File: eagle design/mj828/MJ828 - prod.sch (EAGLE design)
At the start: 34 parts, among them IC1 ATTINY4313-MMH, IC2 PBRC8.00GR50X000, IC3 LDK320M50R, IC4 MCP2515, IC5 MCP2561-2, IC6 MAX6817EUT+T, IC7 MAX6817EUT+T, SW1 TL3305CF160QG, SW2 TL3305CF160QG

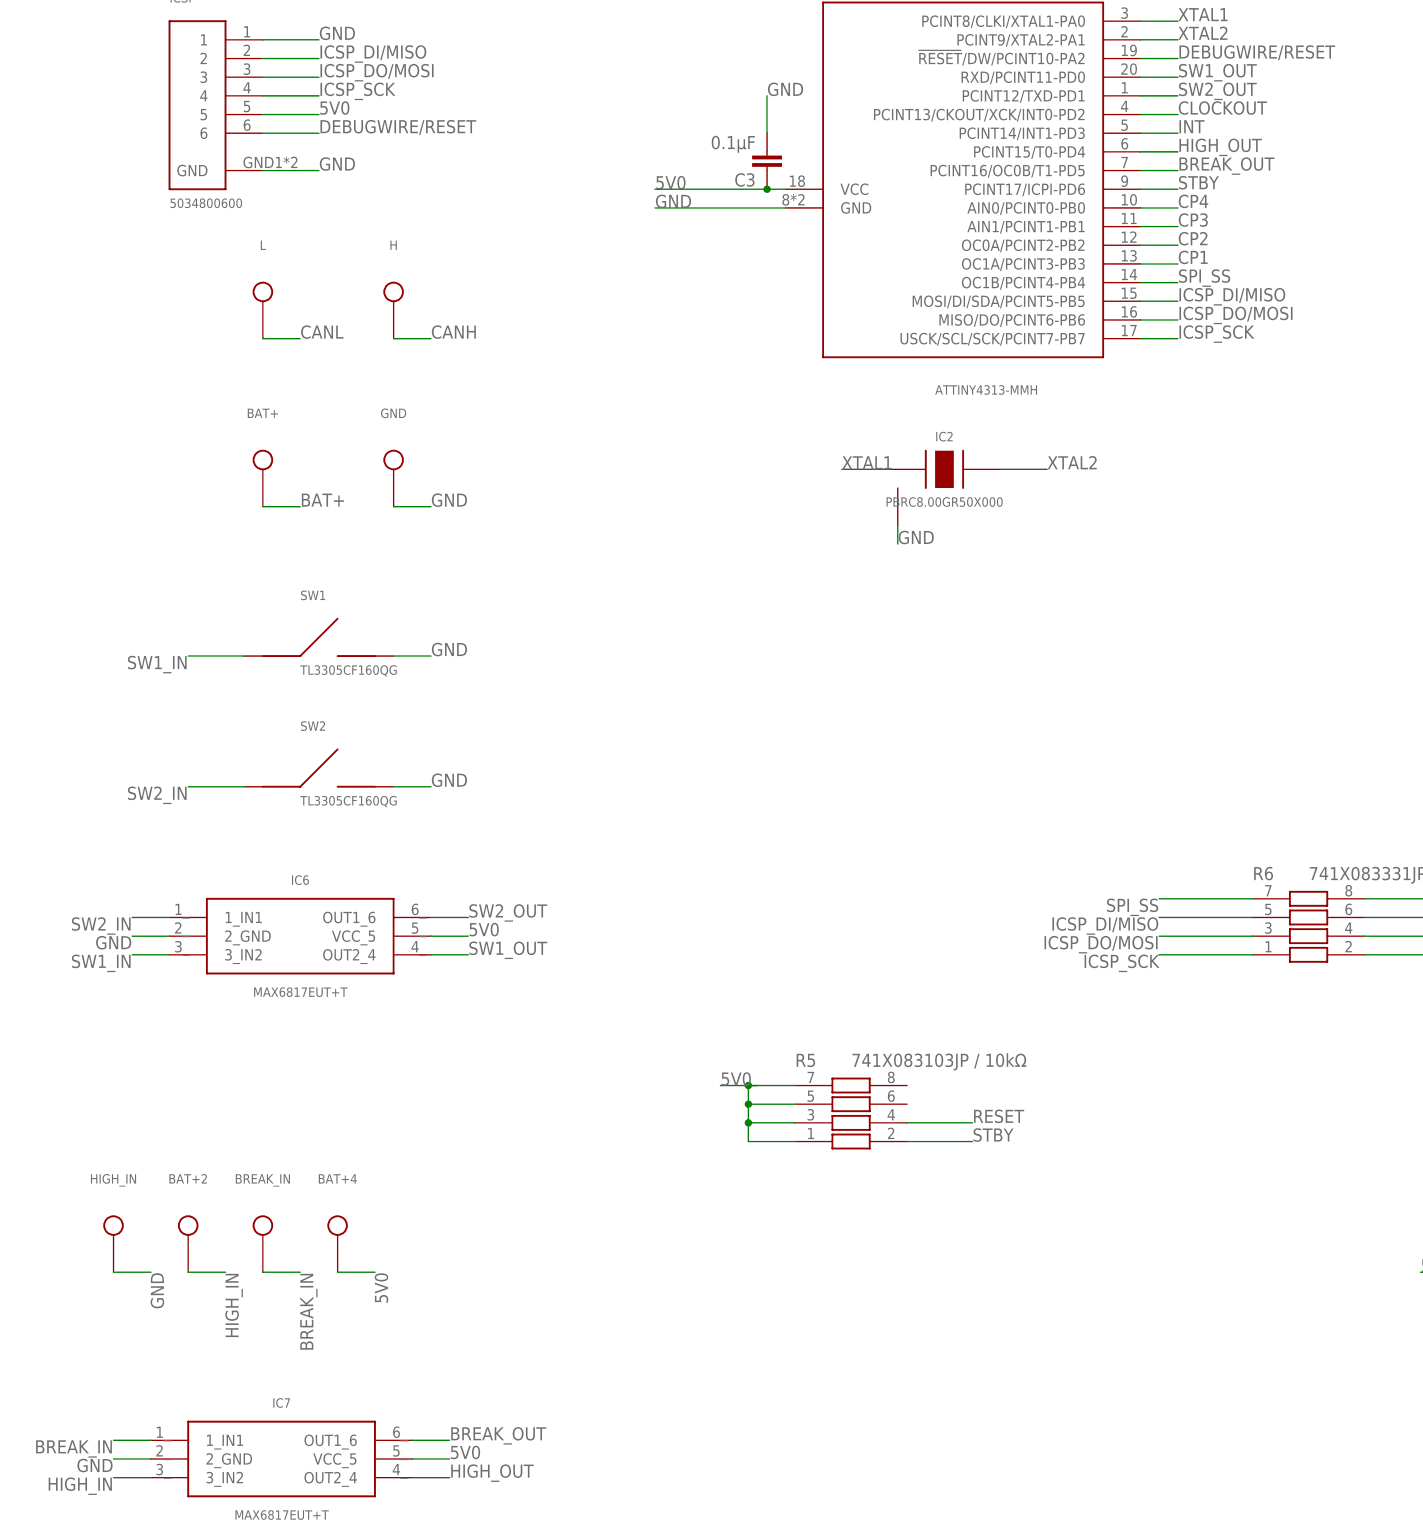
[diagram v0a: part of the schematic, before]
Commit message: MJ828 rev.2 board finished - added 104249/104250 mezzanine connector in order to avoid soldering wires directly onto PCB - drew mezzanine FPC - added datasheets & libraries for molex 104249/104250 mezzanine connectors
replaced hall effect sensor for brake lever FPC
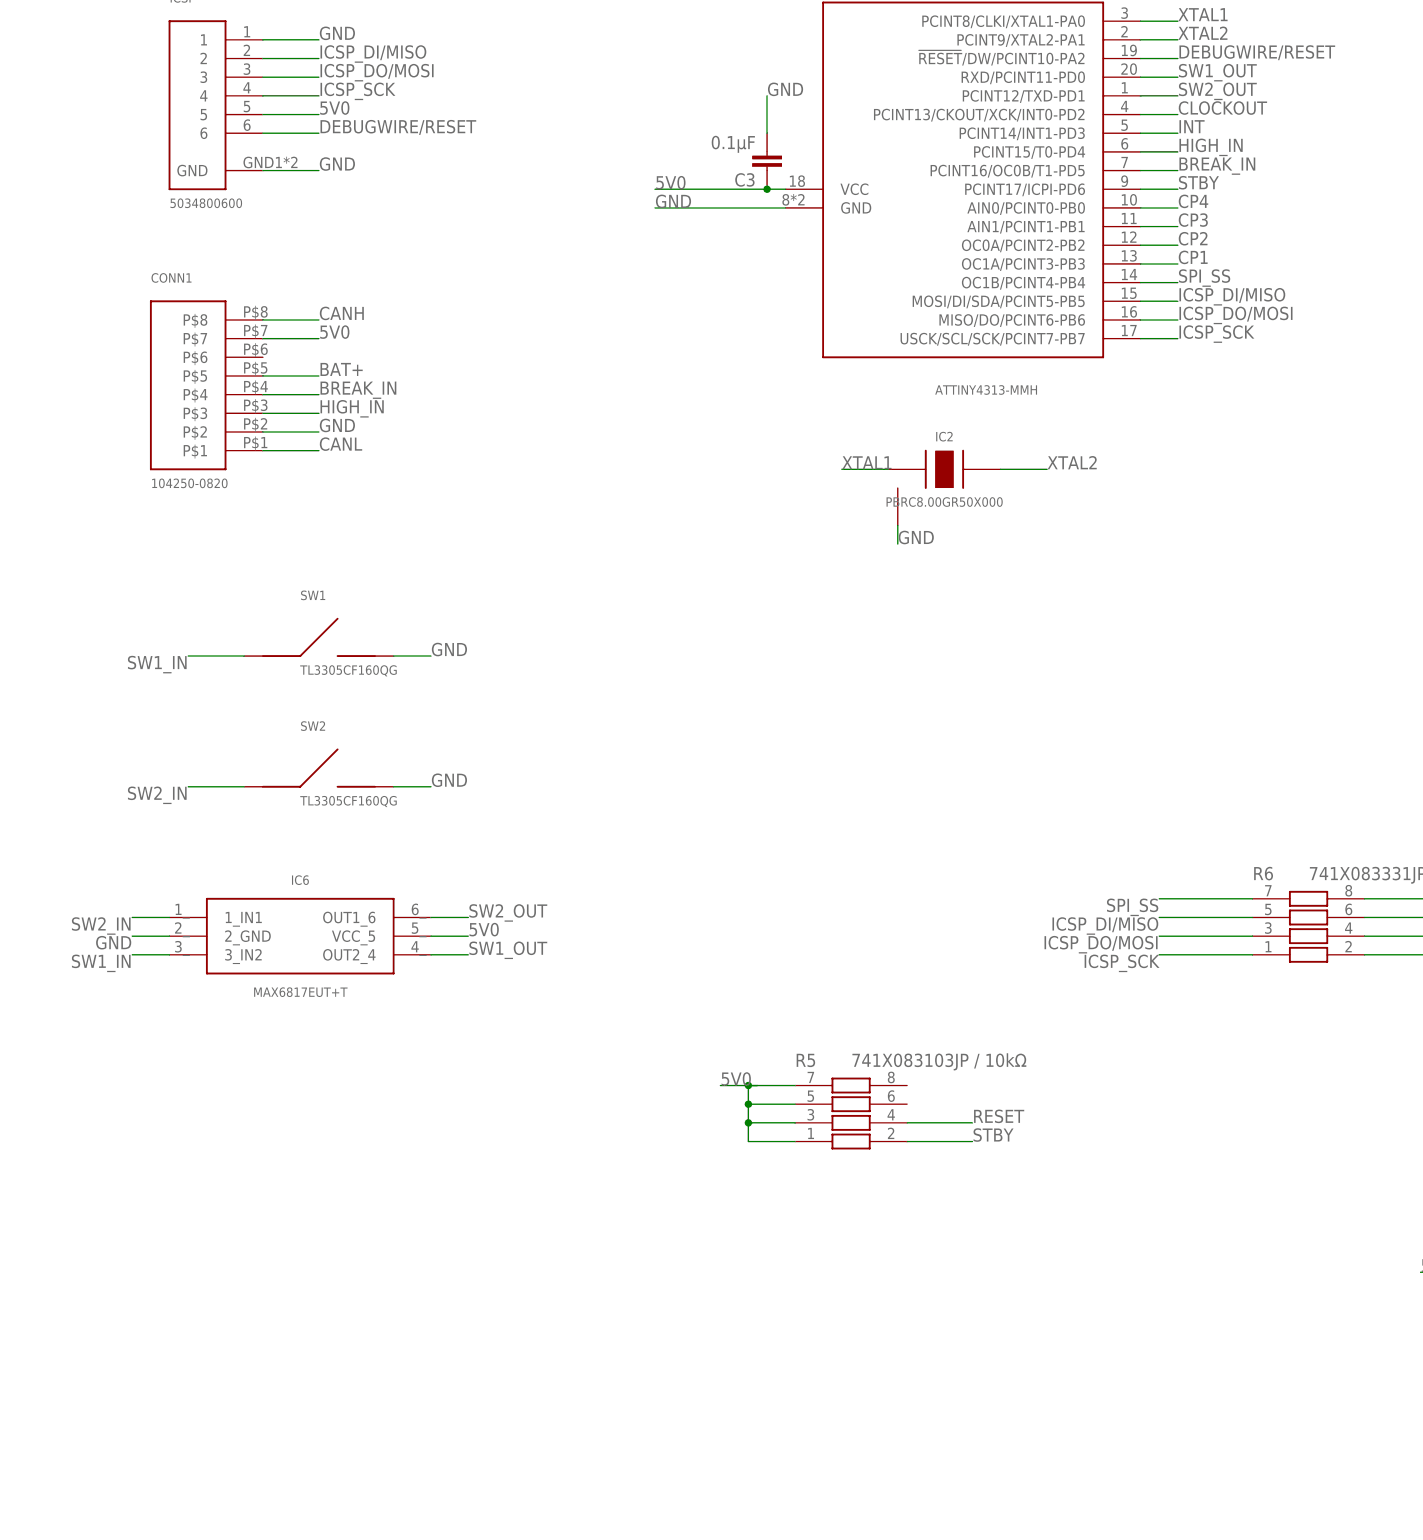
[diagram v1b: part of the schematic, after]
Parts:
- removed BAT+, BAT+2, BAT+4, BREAK_IN, HIGH_IN: 8V4 Battery +, signal testpoint:TPTH-0.9MM
- removed GND: Ground, signal testpoint:TPTH-0.9MM
- removed H: CAN High, signal testpoint:TPTH-0.9MM
- removed IC7: MAX6817EUT+T, MAX6817EUT - CMOS Switch debouncer:MAX6817EUT
- removed L: CAN Low, signal testpoint:TPTH-0.9MM
- added CONN1: 104250-0820, 1042500820 - Board to Board Connector, 8p - Header:104250-0820
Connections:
- removed net BREAK_OUT: IC1.PCINT16/OC0B/T1-PD5, IC7.OUT1_6
- removed net HIGH_OUT: IC1.PCINT15/T0-PD4, IC7.OUT2_4
- net 5V0: now also CONN1.P$7; no longer BAT+4.TP$1, IC7.VCC_5
- net BAT+: now also CONN1.P$5; no longer BAT+.TP$1
- net BREAK_IN: now also CONN1.P$4, IC1.PCINT16/OC0B/T1-PD5; no longer BREAK_IN.TP$1, IC7.1_IN1
- net CANH: now also CONN1.P$8; no longer H.TP$1
- net CANL: now also CONN1.P$1; no longer L.TP$1
- net GND: now also CONN1.P$2; no longer GND.TP$1, HIGH_IN.TP$1, IC7.2_GND
- net HIGH_IN: now also CONN1.P$3, IC1.PCINT15/T0-PD4; no longer BAT+2.TP$1, IC7.3_IN2
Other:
- note removed: "Brake Lever"
- note removed: "CAN bus"
- note removed: "Liion battery - 2S"

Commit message: - replaced 2nd pushbutton with phototransistor, added relevant libraries & datasheets
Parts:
- removed C6: 1μF, rcl:C-EUC0402
- removed C7: 0.1μF, rcl:C-EUC0402
- removed SW2: TL3305CF160QG, TL3305-844809 SPST-NO Tact Switch:TL3305-844809
- added C1, C2: 0.1μF, rcl:C-EUC0402
- added IC7: MCP2561-2, MCP2561-2 - High-Speed CAN Transceiver:MCP2561-2
- added R1: 3312J-1-503E, 3312 - Trim Poti:3312
- C3, C4: value 0.1μF -> 1μF
- C5: value 1μF -> 0.1μF
- IC1: value ATTINY4313-MMH -> SFH 320 FA-Z; device ATtiny4313 microcontroller:ATTINY4313VQFN-20 -> SFH 320 FA - IR Phototransistor:SFH320FA; SPICEPREFIX X -> (none)
- IC2: value PBRC8.00GR50X000 -> MAX6816EUS+T; device PRQV8.00CR1510Y00L - 8MHz resonator:PRQV -> MAX6818 CMOS Switch debouncer:MAX6816
- IC3: value LDK320M50R -> ATTINY4313-MMH; device LDK320 5V LDO:LDK320SOT-23-5L -> ATtiny4313 microcontroller:ATTINY4313VQFN-20; SPICEPREFIX (none) -> X
- IC4: value MCP2515 -> PBRC8.00GR50X000; device MCP2515-I-ML - Standalonce CAN Controller with SPI Interface:MCP2515-I-ML -> PRQV8.00CR1510Y00L - 8MHz resonator:PRQV
- IC5: value MCP2561-2 -> LDK320M50R; device MCP2561-2 - High-Speed CAN Transceiver:MCP2561-2 -> LDK320 5V LDO:LDK320SOT-23-5L
- IC6: value MAX6817EUT+T -> MCP2515; device MAX6817EUT - CMOS Switch debouncer:MAX6817EUT -> MCP2515-I-ML - Standalonce CAN Controller with SPI Interface:MCP2515-I-ML
- renumbered BLUE1 to LED5, BLUE2 to LED3, BLUE3 to LED6, BLUE4 to LED7, BLUE5 to LED8, CONN1 to FPC, GREEN to LED4, R5 to R2, R6 to R3, R8 to R4, RED to LED1, SW1 to SW, YELLOW to LED2
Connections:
- removed net SW1_IN: IC6.3_IN2, SW.P$1
- removed net SW1_OUT: IC1.RXD/PCINT11-PD0, IC6.OUT2_4
- removed net SW2_IN: IC6.1_IN1, SW2.P$1
- removed net SW2_OUT: IC1.PCINT12/TXD-PD1, IC6.OUT1_6
- new net PHOTOTRANSISTOR: IC1.COLLECTOR, IC3.PCINT12/TXD-PD1, R1.3_CW
- new net SW_IN: IC2.2_IN1, SW.P$1
- new net SW_OUT: IC2.OUT1_3, IC3.RXD/PCINT11-PD0
- net 5V0: now also C1.1, C2.1, C4.2, C5.1, IC2.VCC_4, IC3.VCC, IC5.VOUT, IC6.VDD, IC7.VCC, R1.2_WIPER; no longer C3.1, C4.1, C6.2, C7.1, IC1.VCC, IC3.VOUT, IC4.VDD, IC5.VCC, IC6.VCC_5
- net BAT+: now also C3.1, IC5.EN, IC5.VIN; no longer C5.1, IC3.EN, IC3.VIN
- net BREAK_IN: now also IC3.PCINT16/OC0B/T1-PD5; no longer IC1.PCINT16/OC0B/T1-PD5
- net CANH: now also IC7.CANH; no longer IC5.CANH
- net CANL: now also IC7.CANL; no longer IC5.CANL
- net CLOCKOUT: now also IC3.PCINT13/CKOUT/XCK/INT0-PD2, IC6.OSC1; no longer IC1.PCINT13/CKOUT/XCK/INT0-PD2, IC4.OSC1
- net CP1: now also IC3.OC1A/PCINT3-PB3; no longer IC1.OC1A/PCINT3-PB3
- net CP2: now also IC3.OC0A/PCINT2-PB2; no longer IC1.OC0A/PCINT2-PB2
- net CP3: now also IC3.AIN1/PCINT1-PB1; no longer IC1.AIN1/PCINT1-PB1
- net CP4: now also IC3.AIN0/PCINT0-PB0; no longer IC1.AIN0/PCINT0-PB0
- net DEBUGWIRE/RESET: now also IC3.!RESET!/DW/PCINT10-PA2; no longer IC1.!RESET!/DW/PCINT10-PA2
- net GND: now also C1.2, C2.2, C4.1, IC1.EMITTER, IC2.1_GND, IC6.GND, IC7.GND; no longer C4.2, C6.1, C7.2, IC1.GND, IC2.GND, IC6.2_GND, SW2.P$2
- net HIGH_IN: now also IC3.PCINT15/T0-PD4; no longer IC1.PCINT15/T0-PD4
- net ICSP_DI/MISO: now also IC3.MOSI/DI/SDA/PCINT5-PB5; no longer IC1.MOSI/DI/SDA/PCINT5-PB5
- net ICSP_DO/MOSI: now also IC3.MISO/DO/PCINT6-PB6; no longer IC1.MISO/DO/PCINT6-PB6
- net ICSP_SCK: now also IC3.USCK/SCL/SCK/PCINT7-PB7; no longer IC1.USCK/SCL/SCK/PCINT7-PB7
- net INT: now also IC3.PCINT14/INT1-PD3, IC6.!INT!; no longer IC1.PCINT14/INT1-PD3, IC4.!INT!
- net RESET: now also IC6.!RESET!; no longer IC4.!RESET!
- net RXCAN: now also IC6.RXCAN, IC7.RXD; no longer IC4.RXCAN, IC5.RXD
- net SPI_MISO: now also IC6.SO; no longer IC4.SO
- net SPI_MOSI: now also IC6.SI; no longer IC4.SI
- net SPI_SCK: now also IC6.SCK; no longer IC4.SCK
- net SPI_SS: now also IC3.OC1B/PCINT4-PB4, IC6.!CS!; no longer IC1.OC1B/PCINT4-PB4, IC4.!CS!
- net STBY: now also IC3.PCINT17/ICPI-PD6, IC7.STBY; no longer IC1.PCINT17/ICPI-PD6, IC5.STBY
- net TXCAN: now also IC6.TXCAN, IC7.TXD; no longer IC4.TXCAN, IC5.TXD
- net XTAL1: now also IC3.PCINT8/CLKI/XTAL1-PA0, IC4.XTAL1; no longer IC1.PCINT8/CLKI/XTAL1-PA0, IC2.XTAL1
- net XTAL2: now also IC3.PCINT9/XTAL2-PA1, IC4.XTAL2; no longer IC1.PCINT9/XTAL2-PA1, IC2.XTAL2
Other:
- note added: "Phototransistor for daylight detection"
- note added: "Pushbutton"
- note removed: "Pushbuttons"
- moved on the sheet: C3, C4, C5

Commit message: - changed 0804 LEDs to 1206, rerouted, added relevant datasheets - added BOM (includes FPC board to board connector) - created MJ828 autocad housing drawing
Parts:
- removed LED1: HSMS-C170, led:LEDSML0805
- removed LED2: HSMY-C170, led:LEDSML0805
- removed LED3, LED5, LED6, LED7, LED8: HSMN-C170, led:LEDSML0805
- removed LED4: HSMG-C170, led:LEDSML0805
- added LED_BATT1, LED_BATT2, LED_BATT3, LED_BATT4, LED_BLUE: 156120BS82500, led:LEDSML1206
- added LED_GREEN: 156120VS82500, led:LEDSML1206
- added LED_RED: 156120RS82500, led:LEDSML1206
- added LED_YELLOW: 156120YS82500, led:LEDSML1206
- added R5: 741X083101JP / 100Ω, 741X083331JP Resistor Array:741X083331JP
- IC4: value PBRC8.00GR50X000 -> AWSCR-8.00CELA-C10-T3
- R4: value 741X083102JP / 1kΩ -> 741X083151JP / 150Ω
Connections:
- removed net D_Y: LED2.A, LED5.C, R4.5
- removed net N$11: LED3.A, LED6.C, R4.3
- removed net N$12: LED7.C, LED8.A, R4.1
- removed net N$5: LED1.A, LED4.C, R4.7
- new net D_BATT1&2: LED_BATT1.A, LED_BATT2.C, R5.3
- new net D_BATT3&4: LED_BATT3.C, LED_BATT4.A, R5.1
- new net D_BLUE: LED_BLUE.C, R5.5
- new net D_RED&GREEN: LED_GREEN.C, LED_RED.A, R4.7
- new net D_YELLOW: LED_YELLOW.A, R4.1
- net CANH: now also FPC.P$1; no longer FPC.P$8
- net CANL: now also FPC.P$8; no longer FPC.P$1
- net CP1: now also LED_BATT3.A, LED_BATT4.C, LED_GREEN.A, LED_RED.C; no longer LED1.C, LED4.A, LED7.A, LED8.C
- net CP2: now also LED_BLUE.A, LED_YELLOW.C; no longer LED2.C, LED5.A
- net CP3: now also LED_BATT1.C, LED_BATT2.A, R4.2; no longer LED3.C, LED6.A, R4.6
- net CP4: now also R5.2, R5.4, R5.6; no longer R4.2, R4.4
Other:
- note added: "Blue LEDs: Uf = 3.2V, If = 0.02A 5V-3.2V=1.8V 1.8V/0.02A=90Ω rounded to 100Ω"
- note added: "Red, Green, Yellow LEDs: Uf = 2.0V, If = 0.02A 5V-2V=3V 3V/0.02A=150Ω"
- moved on the sheet: R4

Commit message: - updated schematic with phototransistor resistance observation data at dawn
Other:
- note added: "phototransistor: R in darkness in the 1+MΩ range, in full daylight in the <10kΩ range transition to daylight is at around 30kΩ the sun is about to rise bove the horizon, the sky already is casting shadows transition to night is ...."
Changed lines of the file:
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@@
 <text x="231.14" y="195.58" size="1.778" layer="90">power supply for everything</text>
 <text x="261.62" y="78.74" size="1.778" layer="90">CAN infrastructure</text>
-<wire x1="0" y1="228.6" x2="81.28" y2="228.6" width="0.1524" layer="90"/>
+<wire x1="2.54" y1="228.6" x2="81.28" y2="228.6" width="0.1524" layer="90"/>
 <wire x1="81.28" y1="228.6" x2="307.34" y2="228.6" width="0.1524" layer="90"/>
 <wire x1="307.34" y1="228.6" x2="436.88" y2="228.6" width="0.1524" layer="90"/>
@@
 <wire x1="436.88" y1="0" x2="81.28" y2="0" width="0.1524" layer="90"/>
 <wire x1="81.28" y1="0" x2="0" y2="0" width="0.1524" layer="90"/>
-<wire x1="0" y1="0" x2="0" y2="228.6" width="0.1524" layer="90"/>
-<wire x1="81.28" y1="0" x2="81.28" y2="101.6" width="0.1524" layer="90"/>
+<wire x1="81.28" y1="0" x2="81.28" y2="76.2" width="0.1524" layer="90"/>
+<wire x1="81.28" y1="76.2" x2="81.28" y2="101.6" width="0.1524" layer="90"/>
 <wire x1="81.28" y1="101.6" x2="307.34" y2="101.6" width="0.1524" layer="90"/>
 <wire x1="436.88" y1="101.6" x2="307.34" y2="101.6" width="0.1524" layer="90"/>
@@
 1.8V/0.02A=90Ω
 rounded to 100Ω</text>
+<text x="-53.34" y="58.42" size="1.778" layer="91" align="top-left">phototransistor:
+    R in darkness in the 1+MΩ range,
+    in full daylight in the &lt;10kΩ range
+transition to daylight is at around 30kΩ
+    the sun is about to rise bove the horizon,
+    the sky already is casting shadows
+transition to night is ....</text>
+<wire x1="0" y1="0" x2="-76.2" y2="0" width="0.1524" layer="90"/>
+<wire x1="-76.2" y1="0" x2="-76.2" y2="76.2" width="0.1524" layer="90"/>
+<wire x1="-76.2" y1="76.2" x2="0" y2="76.2" width="0.1524" layer="90"/>
+<wire x1="0" y1="76.2" x2="81.28" y2="76.2" width="0.1524" layer="90"/>
+<wire x1="0" y1="76.2" x2="0" y2="228.6" width="0.1524" layer="90"/>
+<wire x1="0" y1="228.6" x2="2.54" y2="228.6" width="0.1524" layer="90"/>
 </plain>
 <instances>

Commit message: - updated schematic with phototransistor resistance observation data at dusk
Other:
- note added: "TODO: pulldown for brake/high beam signals"
- note added: "nighttime: R > 1MΩ daylight: R<15kΩ"
- note added: "phototransistor: R in darkness in the >1MΩ range, in full daylight in the <10kΩ range transition to daylight is at around 25-30kΩ the sun is about to rise bove the horizon, the sky already is casting shadows at ~20kΩ the sun is already above the horizon transition to night is ...."
- note removed: "phototransistor: R in darkness in the 1+MΩ range, in full daylight in the <10kΩ range transition to daylight is at around 30kΩ the sun is about to rise bove the horizon, the sky already is casting shadows transition to night is ...."
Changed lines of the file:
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@@
 rounded to 100Ω</text>
 <text x="-53.34" y="58.42" size="1.778" layer="91" align="top-left">phototransistor:
-    R in darkness in the 1+MΩ range,
+    R in darkness in the &gt;1MΩ range,
     in full daylight in the &lt;10kΩ range
-transition to daylight is at around 30kΩ
+transition to daylight is at around 25-30kΩ
     the sun is about to rise bove the horizon,
     the sky already is casting shadows
+at ~20kΩ the sun is already above the horizon
 transition to night is ....</text>
 <wire x1="0" y1="0" x2="-76.2" y2="0" width="0.1524" layer="90"/>
@@
 <wire x1="0" y1="76.2" x2="0" y2="228.6" width="0.1524" layer="90"/>
 <wire x1="0" y1="228.6" x2="2.54" y2="228.6" width="0.1524" layer="90"/>
+<text x="170.18" y="180.34" size="5.08" layer="90">TODO: pulldown for brake/high beam signals</text>
+<text x="43.18" y="40.64" size="1.9304" layer="91">nighttime: R &gt; 1MΩ
+daylight: R&lt;15kΩ</text>
 </plain>
 <instances>
